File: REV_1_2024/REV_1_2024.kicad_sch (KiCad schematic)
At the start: 1 part, among them U1 Teensy4.1_DEV-16771

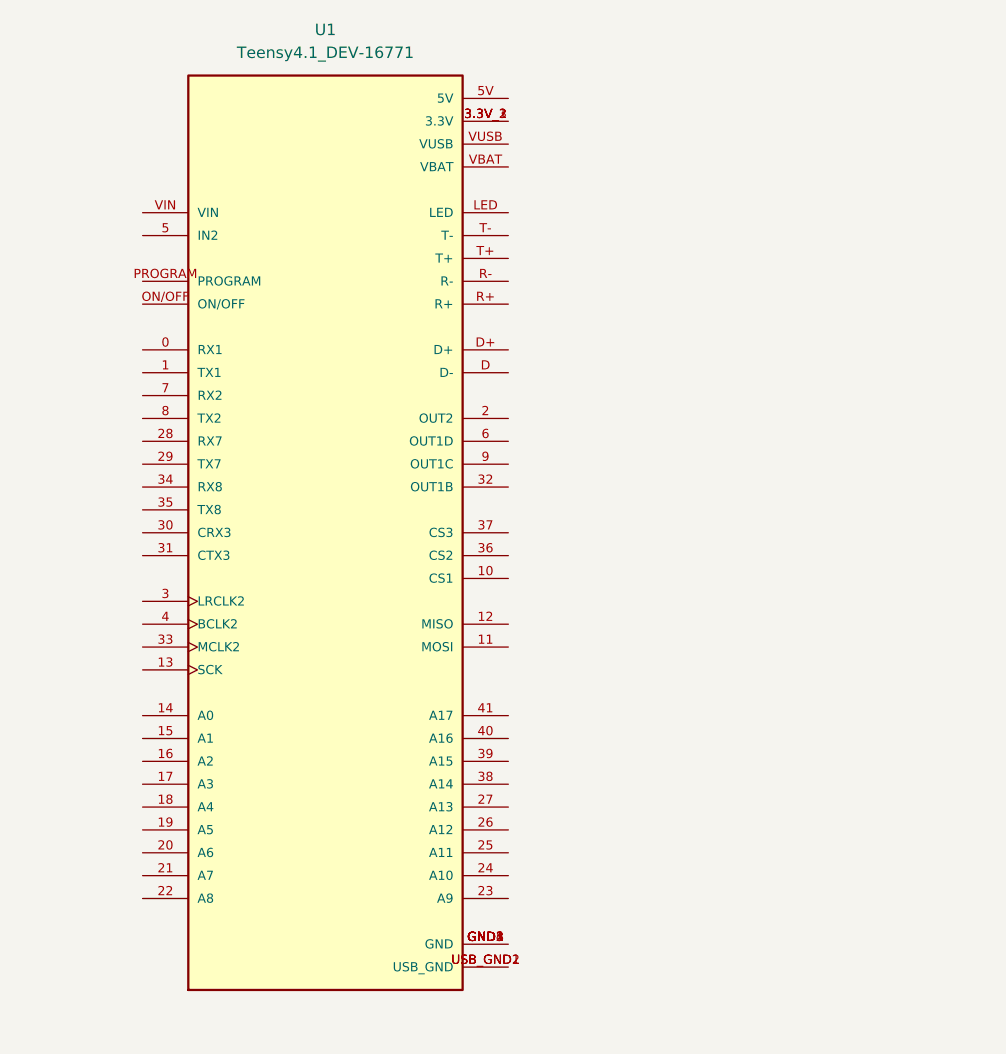
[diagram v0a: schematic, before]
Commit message: added ethernet
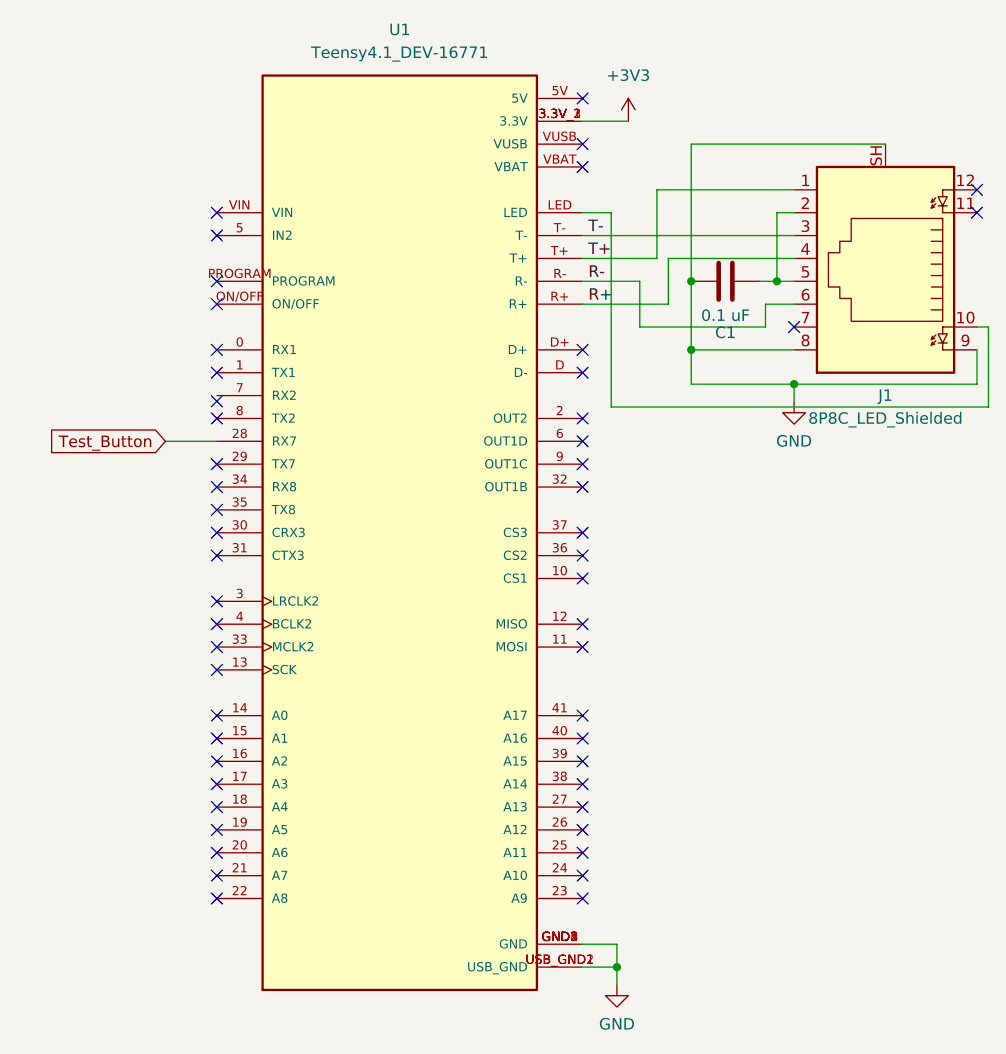
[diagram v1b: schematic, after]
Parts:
- added C1: 0.1 uF, symbol Device:C
- added J1: 8P8C_LED_Shielded, symbol Connector:8P8C_LED_Shielded
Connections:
- net Test_Button: now reaches U1.28 (RX7)
- net +3V3: now reaches U1.3.3V_1 (3.3V), U1.3.3V_2 (3.3V), U1.3.3V_3 (3.3V)
- net GND: now reaches U1.GND1 (GND), U1.GND2 (GND), U1.GND3 (GND), U1.GND4 (GND), U1.GND5 (GND)
- net GND: now also U1.USB_GND1 (USB_GND), U1.USB_GND2 (USB_GND), C1.2, J1.8, J1.9, J1.SH
- net at U1.LED: now also J1.10
- net R+: now reaches U1.R+
- net R+: now also J1.4
- net R-: now reaches U1.R-
- net R-: now also J1.6
- net T+: now reaches U1.T+
- net T+: now also J1.1
- net T-: now reaches U1.T-
- net T-: now also J1.3
- new net: C1.1, J1.2, J1.5
- no-connect marks 0 -> 52

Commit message: Schematic Created
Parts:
- removed J1: 8P8C_LED_Shielded, symbol Connector:8P8C_LED_Shielded
- removed U1: Teensy4.1_DEV-16771, MODULE_DEV-16771, symbol MRDT_Shields:Teensy4.1_DEV-16771
- added C2, C3: 1uF, Capacitor_SMD:C_0603_1608Metric_Pad1.08x0.95mm_HandSolder, symbol Device:C
- added C4, C5: 220uF, Capacitor_SMD:C_0603_1608Metric_Pad1.08x0.95mm_HandSolder, symbol Device:C
- added Conn1, Conn2: AndersonPP, symbol MRDT_Connectors:AndersonPP
- added Conn3: Molex_SL_03, MRDT_Connectors:MOLEX_SL_03_Vertical, symbol MRDT_Connectors:Molex_SL_03
- added D1, D3: Orange, LED_SMD:LED_0603_1608Metric_Pad1.05x0.95mm_HandSolder, symbol Device:LED
- added D2, D4: SD0603S04, Diode_SMD:D_0603_1608Metric_Pad1.05x0.95mm_HandSolder, symbol Device:D
- added Q1, Q2, Q3, Q4: Si4156DY, Package_SO:SOIC-8_3.9x4.9mm_P1.27mm, symbol Transistor_FET:Si4162DY
- added R1, R4: 120, Resistor_SMD:R_0603_1608Metric_Pad0.98x0.95mm_HandSolder, symbol Device:R
- added R2, R3, R5, R6: 100, Resistor_SMD:R_0603_1608Metric_Pad0.98x0.95mm_HandSolder, symbol Device:R
- added U1, U4: 74LVC2G04, Package_TO_SOT_SMD:SOT-23-6_Handsoldering, symbol 74xGxx:74LVC2G04
- added U2, U3: IRS2005S, Package_SO:SOIC-8_3.9x4.9mm_P1.27mm, symbol Driver_FET:IRS2005S
- C1: value 0.1 uF -> 10uF; footprint (none) -> Capacitor_SMD:C_0603_1608Metric_Pad1.08x0.95mm_HandSolder
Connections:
- net +3V3: now also Conn3.3, U4.5 (VCC)
- net GND: now also C4.1, C5.1, Conn2.1 (GND), Q2.1 (S), Q2.2 (S), Q2.3 (S), Q4.1 (S), Q4.2 (S), Q4.3 (S), R1.2, R4.2, U2.4 (COM), U3.4 (COM), U4.2 (GND); no longer C1.2
- net M+: now reaches C1.1
- net M+: now also C2.2, Conn1.1 (GND), Q1.1 (S), Q1.2 (S), Q1.3 (S), Q2.5 (D), Q2.6 (D), Q2.7 (D), Q2.8 (D), U2.6 (VS)
- new net: R3.1, U2.5 (LO)
- new net: Q2.4 (G), R3.2
- new net: D1.1 (K), R1.1
- new net: Q4.4 (G), R6.2
- new net: R6.1, U3.5 (LO)
- new net: D1.2 (A), U1.6, U2.2 (HIN)
- new net: C2.1, D2.1 (K), U2.8 (VB)
- new net: C3.1, D4.1 (K), U3.8 (VB)
- new net: Q1.4 (G), R2.2
- new net: D3.1 (K), R4.1
- new net: D3.2 (A), U1.4, U3.2 (HIN)
- new net: R5.1, U3.7 (HO)
- new net: Q3.4 (G), R5.2
- new net: R2.1, U2.7 (HO)
- new net +12V: C4.2, C5.2, Conn2.2 (V+Log), D2.2 (A), D4.2 (A), Q1.5 (D), Q1.6 (D), Q1.7 (D), Q1.8 (D), Q3.5 (D), Q3.6 (D), Q3.7 (D), Q3.8 (D), U2.1 (VCC), U3.1 (VCC)
- new net M-: C3.2, Conn1.2 (V+Log), Q3.1 (S), Q3.2 (S), Q3.3 (S), Q4.5 (D), Q4.6 (D), Q4.7 (D), Q4.8 (D), U3.6 (VS)
- new net PWM_FWD: U1.1, U2.3 (LIN)
- new net PWM_RVS: Conn3.1, Conn3.2, U1.3, U3.3 (LIN)
- no-connect marks 52 -> 0

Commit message: Circuit improvements
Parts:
- removed U2: IRS2005S, Package_SO:SOIC-8_3.9x4.9mm_P1.27mm, symbol Driver_FET:IRS2005S
- added U5: IRS2308, symbol Driver_FET:IRS2308
- R1: value 120 -> 100
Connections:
- net +12V: now also Conn2.3 (V+Act); no longer Conn2.2 (V+Log)
- net M-: now also Conn1.3 (V+Act); no longer Conn1.2 (V+Log)
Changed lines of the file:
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@@
   (junction (at 219.71 60.325) (diameter 0) (color 0 0 0 0)
   )
-  (junction (at 80.645 50.165) (diameter 0) (color 0 0 0 0)
-  )
   (junction (at 113.03 36.83) (diameter 0) (color 0 0 0 0)
   )
@@
     (stroke (width 0) (type default))
   )
-  (wire (pts (xy 80.645 50.165) (xy 93.98 50.165))
+  (wire (pts (xy 80.01 50.165) (xy 93.98 50.165))
     (stroke (width 0) (type default))
   )
@@
   )
   (wire (pts (xy 176.53 92.71) (xy 176.53 96.52))
-    (stroke (width 0) (type default))
-  )
-  (wire (pts (xy 80.01 50.165) (xy 80.645 50.165))
     (stroke (width 0) (type default))
   )
@@
       (effects (font (size 1.27 1.27)) (justify left))
     )
-    (property "Value" "120" (at 58.42 74.295 0)
+    (property "Value" "100" (at 58.42 74.295 0)
       (effects (font (size 1.27 1.27)) (justify left))
     )
@@
     )
   )
-  (symbol (lib_id "Driver_FET:IRS2005S") (at 73.025 55.245 0) (unit 1)
-    (in_bom yes) (on_board yes) (dnp no) (fields_autoplaced)
-    (property "Reference" "U2" (at 75.2191 40.64 0)
-      (effects (font (size 1.27 1.27)) (justify left))
-    )
-    (property "Value" "IRS2005S" (at 75.2191 43.18 0)
-      (effects (font (size 1.27 1.27)) (justify left))
-    )
-    (property "Footprint" "Package_SO:SOIC-8_3.9x4.9mm_P1.27mm" (at 73.025 55.245 0)
+  (symbol (lib_id "power:GND") (at 162.56 99.06 0) (unit 1)
+    (in_bom yes) (on_board yes) (dnp no) (fields_autoplaced)
+    (property "Reference" "#PWR09" (at 162.56 105.41 0)
+      (effects (font (size 1.27 1.27)) hide)
+    )
+    (property "Value" "GND" (at 162.56 103.505 0)
+      (effects (font (size 1.27 1.27)))
+    )
+    (property "Footprint" "" (at 162.56 99.06 0)
+      (effects (font (size 1.27 1.27)) hide)
+    )
+    (property "Datasheet" "" (at 162.56 99.06 0)
+      (effects (font (size 1.27 1.27)) hide)
+    )
+    (pin "1")
+    (instances
+      (project "REV_1_2024"
+        (path "/09f10023-b6cf-44c5-8847-9c4a76610e70"
+          (reference "#PWR09") (unit 1)
+        )
+      )
+    )
+  )
+  (symbol (lib_id "power:GND") (at 73.025 78.74 0) (unit 1)
+    (in_bom yes) (on_board yes) (dnp no) (fields_autoplaced)
+    (property "Reference" "#PWR01" (at 73.025 85.09 0)
+      (effects (font (size 1.27 1.27)) hide)
+    )
+    (property "Value" "GND" (at 73.025 83.185 0)
+      (effects (font (size 1.27 1.27)))
+    )
+    (property "Footprint" "" (at 73.025 78.74 0)
+      (effects (font (size 1.27 1.27)) hide)
+    )
+    (property "Datasheet" "" (at 73.025 78.74 0)
+      (effects (font (size 1.27 1.27)) hide)
+    )
+    (pin "1")
+    (instances
+      (project "REV_1_2024"
+        (path "/09f10023-b6cf-44c5-8847-9c4a76610e70"
+          (reference "#PWR01") (unit 1)
+        )
+      )
+    )
+  )
+  (symbol (lib_id "Driver_FET:IRS2308") (at 72.898 55.372 0) (unit 1)
+    (in_bom yes) (on_board yes) (dnp no) (fields_autoplaced)
+    (property "Reference" "U5" (at 75.0921 39.878 0)
+      (effects (font (size 1.27 1.27)) (justify left))
+    )
+    (property "Value" "IRS2308" (at 75.0921 42.418 0)
+      (effects (font (size 1.27 1.27)) (justify left))
+    )
+    (property "Footprint" "" (at 72.898 55.372 0)
       (effects (font (size 1.27 1.27) italic) hide)
     )
-    (property "Datasheet" "https://www.infineon.com/dgdl/Infineon-IRS2005S-DS-v02_00-EN.pdf?fileId=5546d462533600a4015364c4246229e1" (at 73.025 55.245 0)
+    (property "Datasheet" "https://www.infineon.com/dgdl/irs2308.pdf?fileId=5546d462533600a40153567a98ac2804" (at 72.898 55.372 0)
       (effects (font (size 1.27 1.27)) hide)
     )
@@
       (project "REV_1_2024"
         (path "/09f10023-b6cf-44c5-8847-9c4a76610e70"
-          (reference "U2") (unit 1)
-        )
-      )
-    )
-  )
-  (symbol (lib_id "power:GND") (at 162.56 99.06 0) (unit 1)
-    (in_bom yes) (on_board yes) (dnp no) (fields_autoplaced)
-    (property "Reference" "#PWR09" (at 162.56 105.41 0)
-      (effects (font (size 1.27 1.27)) hide)
-    )
-    (property "Value" "GND" (at 162.56 103.505 0)
-      (effects (font (size 1.27 1.27)))
-    )
-    (property "Footprint" "" (at 162.56 99.06 0)
-      (effects (font (size 1.27 1.27)) hide)
-    )
-    (property "Datasheet" "" (at 162.56 99.06 0)
-      (effects (font (size 1.27 1.27)) hide)
-    )
-    (pin "1")
-    (instances
-      (project "REV_1_2024"
-        (path "/09f10023-b6cf-44c5-8847-9c4a76610e70"
-          (reference "#PWR09") (unit 1)
-        )
-      )
-    )
-  )
-  (symbol (lib_id "power:GND") (at 73.025 78.74 0) (unit 1)
-    (in_bom yes) (on_board yes) (dnp no) (fields_autoplaced)
-    (property "Reference" "#PWR01" (at 73.025 85.09 0)
-      (effects (font (size 1.27 1.27)) hide)
-    )
-    (property "Value" "GND" (at 73.025 83.185 0)
-      (effects (font (size 1.27 1.27)))
-    )
-    (property "Footprint" "" (at 73.025 78.74 0)
-      (effects (font (size 1.27 1.27)) hide)
-    )
-    (property "Datasheet" "" (at 73.025 78.74 0)
-      (effects (font (size 1.27 1.27)) hide)
-    )
-    (pin "1")
-    (instances
-      (project "REV_1_2024"
-        (path "/09f10023-b6cf-44c5-8847-9c4a76610e70"
-          (reference "#PWR01") (unit 1)
+          (reference "U5") (unit 1)
         )
       )
@@
     )
   )
-  (symbol (lib_id "MRDT_Connectors:AndersonPP") (at 147.32 84.455 0) (unit 2)
+  (symbol (lib_id "MRDT_Connectors:AndersonPP") (at 147.32 84.455 0) (unit 3)
     (in_bom yes) (on_board yes) (dnp no) (fields_autoplaced)
     (property "Reference" "Conn2" (at 149.86 74.93 0)
@@
       (project "REV_1_2024"
         (path "/09f10023-b6cf-44c5-8847-9c4a76610e70"
-          (reference "Conn2") (unit 2)
-        )
-      )
-    )
-  )
-  (symbol (lib_id "MRDT_Connectors:AndersonPP") (at 160.655 59.055 0) (unit 2)
+          (reference "Conn2") (unit 3)
+        )
+      )
+    )
+  )
+  (symbol (lib_id "MRDT_Connectors:AndersonPP") (at 160.655 59.055 0) (unit 3)
     (in_bom yes) (on_board yes) (dnp no) (fields_autoplaced)
     (property "Reference" "Conn1" (at 163.195 48.895 0)
@@
       (project "REV_1_2024"
         (path "/09f10023-b6cf-44c5-8847-9c4a76610e70"
-          (reference "Conn1") (unit 2)
-        )
-      )
+          (reference "Conn1") (unit 3)
+        )
+      )
